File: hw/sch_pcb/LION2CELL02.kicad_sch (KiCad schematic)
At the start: 61 parts, among them J1 JUMP_4X2, J13 JUMP_4X2, J15 CONN_2, J2 JUMP_2x1, J3 JUMP_2x1, J4 JUMP2_2x1, J5 JUMP_2x1, J6 JUMP_2x1, J7 JUMP_4X2, J8 CONN1_1, J9 CONN1_1, P1 _, P2 _, P3 _, P4 _, Q1 IRLML6244, U1 BQ29209, U2 BQ24103, U5 TPS76601, U6 APX810-31SAG-7

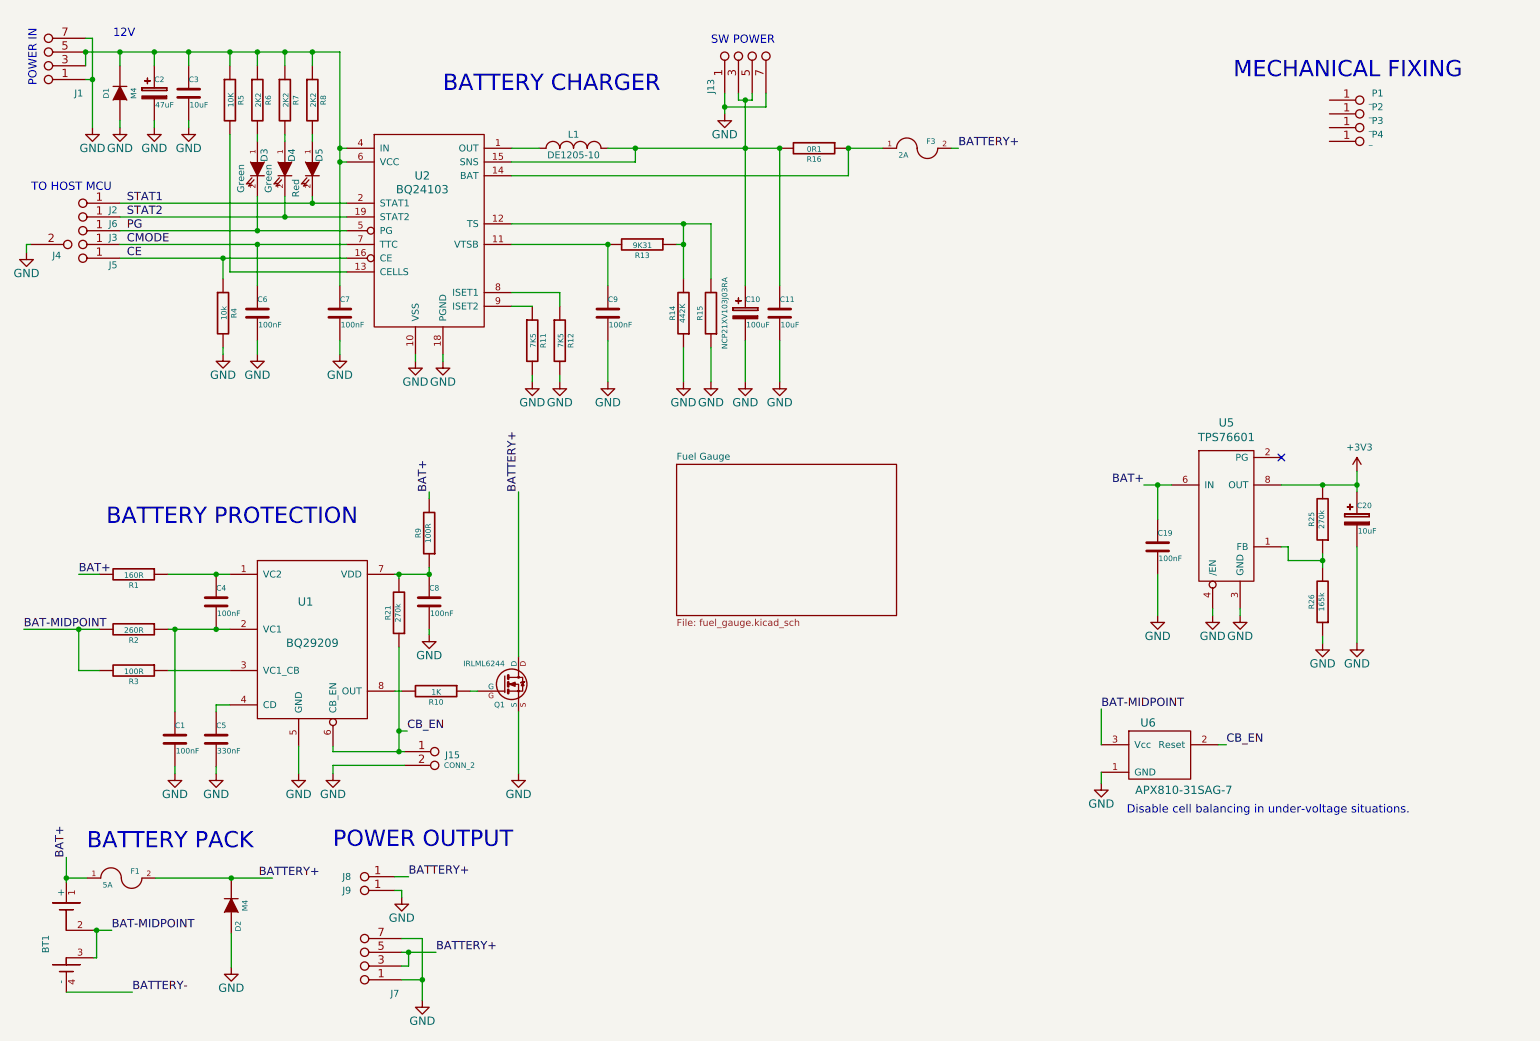
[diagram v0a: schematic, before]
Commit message: Initial work on battery charging.
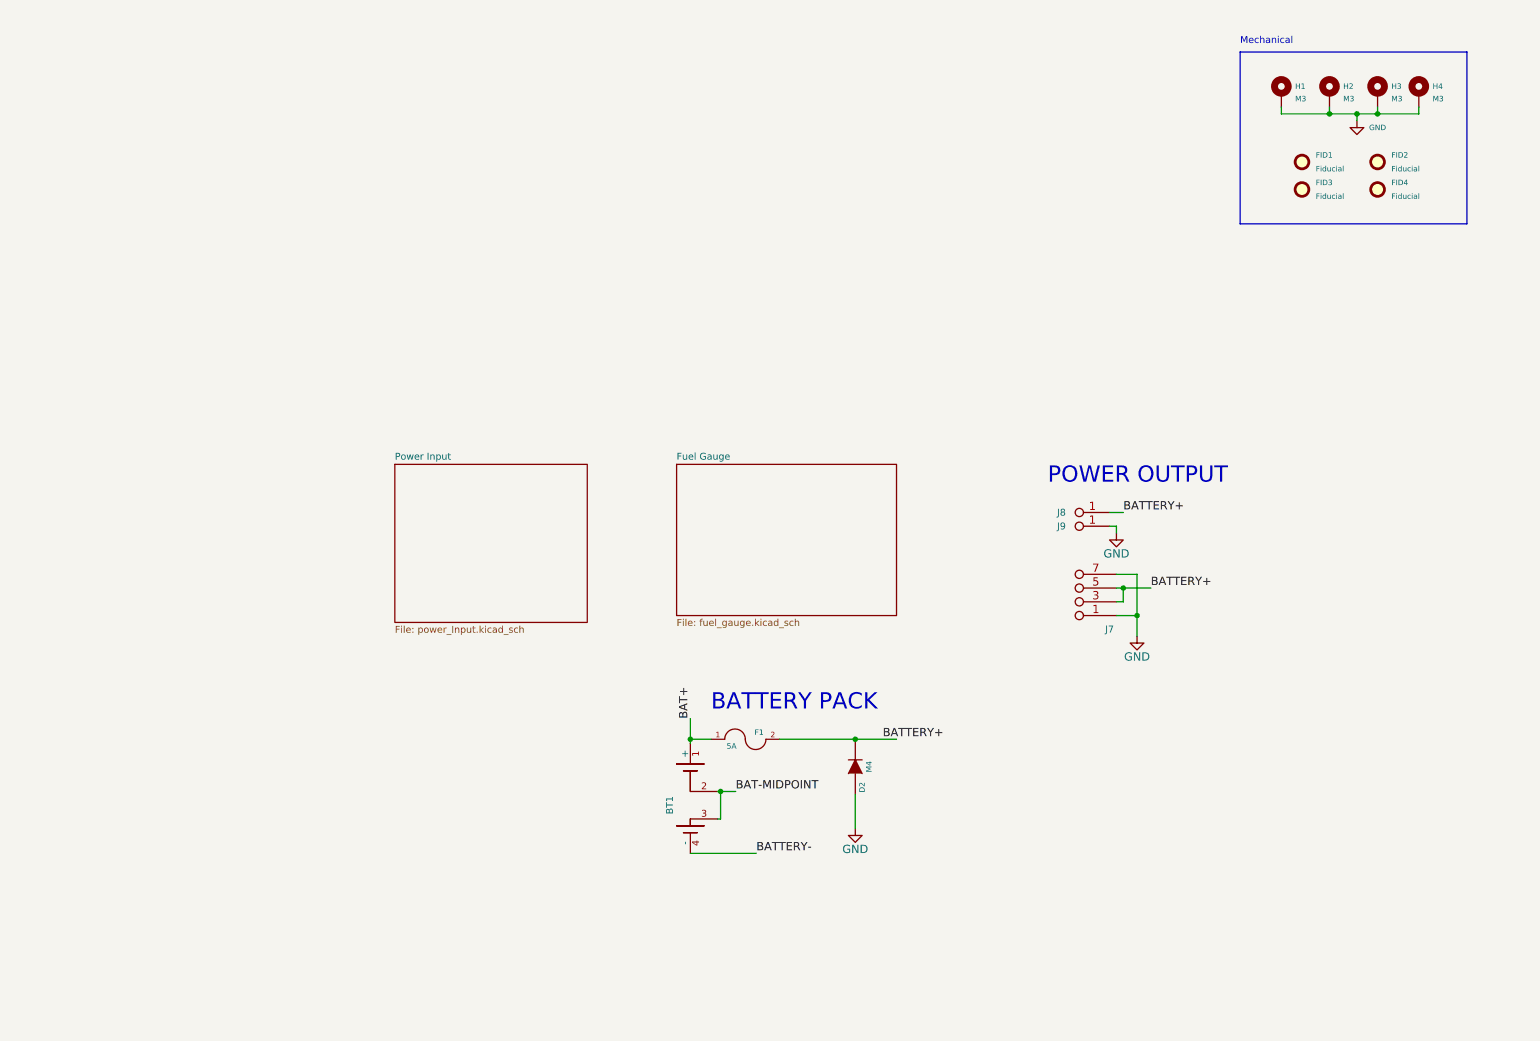
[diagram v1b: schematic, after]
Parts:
- removed C1, C19, C4, C6, C7, C8, C9: 100nF, Mlab_R:SMD-0805, symbol LION2CELL01D-rescue:C-RESCUE-LION2CELL01C
- removed C10: 100uF, Mlab_C:TantalC_SizeD_Reflow, symbol LION2CELL01D-rescue:CP2
- removed C11, C3: 10uF, Mlab_R:SMD-0805, symbol LION2CELL01D-rescue:C-RESCUE-LION2CELL01C
- removed C2: 47uF, Mlab_C:TantalC_SizeC_Reflow, symbol LION2CELL01D-rescue:CP2
- removed C20: 10uF, Mlab_C:TantalC_SizeB_Reflow, symbol LION2CELL01D-rescue:CP2
- removed C5: 330nF, Mlab_R:SMD-0805, symbol LION2CELL01D-rescue:C-RESCUE-LION2CELL01C
- removed D1: M4, Mlab_D:SMA_Standard, symbol LION2CELL01D-rescue:DIODE
- removed D3, D4: Green, Mlab_D:LED_1206, symbol LION2CELL01D-rescue:LED-RESCUE-LION2CELL01C
- removed D5: Red, Mlab_D:LED_1206, symbol LION2CELL01D-rescue:LED-RESCUE-LION2CELL01C
- removed F3: 2A, Mlab_F:Drzak_2410, symbol LION2CELL01D-rescue:FUSE
- removed J1, J13: JUMP_4X2, Mlab_Pin_Headers:Straight_2x04, symbol LION2CELL01D-rescue:JUMP_4X2
- removed J15: CONN_2, Mlab_Pin_Headers:SMD_1_2x2, symbol LION2CELL01D-rescue:CONN_2
- removed J2, J3, J5, J6: JUMP_2x1, Mlab_Pin_Headers:Straight_1x02, symbol LION2CELL01D-rescue:JUMP_2x1
- removed J4: JUMP2_2x1, symbol LION2CELL01D-rescue:JUMP2_2x1
- removed L1: DE1205-10, Mlab_L:DE1205-10, symbol LION2CELL01D-rescue:INDUCTOR_SMALL
- removed P1, P2, P3, P4: _, Mlab_Mechanical:MountingHole_3mm, symbol LION2CELL01D-rescue:_
- removed Q1: IRLML6244, Mlab_T:SOT-23, symbol LION2CELL01D-rescue:MOSFET-N
- removed R1: 160R, Mlab_R:SMD-0805, symbol LION2CELL01D-rescue:R-RESCUE-LION2CELL01C
- removed R10: 1K, Mlab_R:SMD-0805, symbol LION2CELL01D-rescue:R-RESCUE-LION2CELL01C
- removed R11, R12: 7K5, Mlab_R:SMD-0805, symbol LION2CELL01D-rescue:R-RESCUE-LION2CELL01C
- removed R13: 9K31, Mlab_R:SMD-0805, symbol LION2CELL01D-rescue:R-RESCUE-LION2CELL01C
- removed R14: 442K, Mlab_R:SMD-0805, symbol LION2CELL01D-rescue:R-RESCUE-LION2CELL01C
- removed R15: NCP21XV103J03RA, Mlab_R:SMD-0805, symbol LION2CELL01D-rescue:R-RESCUE-LION2CELL01C
- removed R16: 0R1, Resistors_SMD:R_2512, symbol LION2CELL01D-rescue:R-RESCUE-LION2CELL01C
- removed R2: 260R, Mlab_R:SMD-0805, symbol LION2CELL01D-rescue:R-RESCUE-LION2CELL01C
- removed R21, R25: 270k, Mlab_R:SMD-0805, symbol LION2CELL01D-rescue:R-RESCUE-LION2CELL01C
- removed R26: 165k, Mlab_R:SMD-0805, symbol LION2CELL01D-rescue:R-RESCUE-LION2CELL01C
- removed R3, R9: 100R, Mlab_R:SMD-0805, symbol LION2CELL01D-rescue:R-RESCUE-LION2CELL01C
- removed R4: 10k, Mlab_R:SMD-0805, symbol LION2CELL01D-rescue:R-RESCUE-LION2CELL01C
- removed R5: 10K, Mlab_R:SMD-0805, symbol LION2CELL01D-rescue:R-RESCUE-LION2CELL01C
- removed R6, R7, R8: 2K2, Mlab_R:SMD-0805, symbol LION2CELL01D-rescue:R-RESCUE-LION2CELL01C
- removed U1: BQ29209, Mlab_IO:VSON-8, symbol LION2CELL01D-rescue:BQ29209
- removed U2: BQ24103, Mlab_IO:VQFN-20, symbol LION2CELL01D-rescue:BQ24103
- removed U5: TPS76601, Mlab_IO:SO-8, symbol LION2CELL01D-rescue:TPS76601
- removed U6: APX810-31SAG-7, Mlab_IO:SOT-23, symbol LION2CELL01D-rescue:APX810-31SAG-7
- added FID1, FID2, FID3, FID4: Fiducial, Fiducial:Fiducial_1mm_Mask2mm, symbol Mechanical:Fiducial
- added H1, H2, H3, H4: M3, Mlab_Mechanical:MountingHole_3mm, symbol Mechanical:MountingHole_Pad
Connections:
- net GND: now also H1.1, H2.1, H3.1, H4.1
- no-connect marks 1 -> 0
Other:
- added sheet Power Input (power_Input.kicad_sch)
- note added: "Mechanical"
- note removed: "12V"
- note removed: "BATTERY CHARGER"
- note removed: "BATTERY PROTECTION"
- note removed: "Disable cell balancing in under-voltage situations."
- note removed: "MECHANICAL FIXING"
- note removed: "POWER IN"
- note removed: "SW POWER"
- note removed: "TO HOST MCU"
- moved on the sheet: BT1, D2, F1, J7, J8, J9

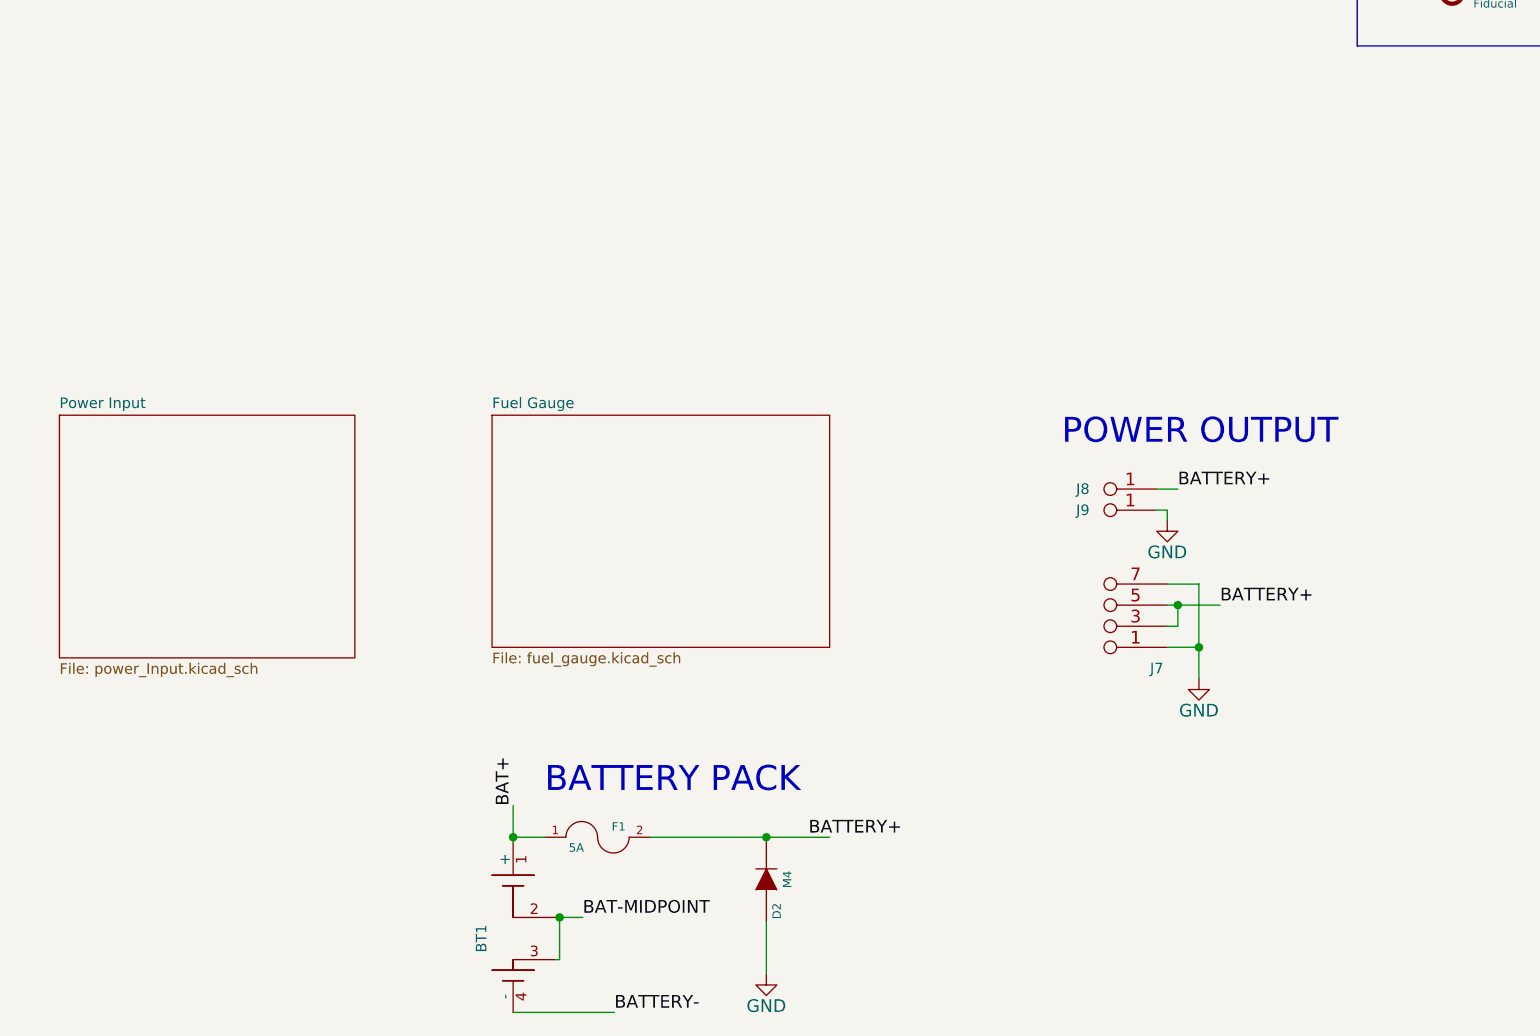
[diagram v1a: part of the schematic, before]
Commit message: work of the schematics of charger completed.
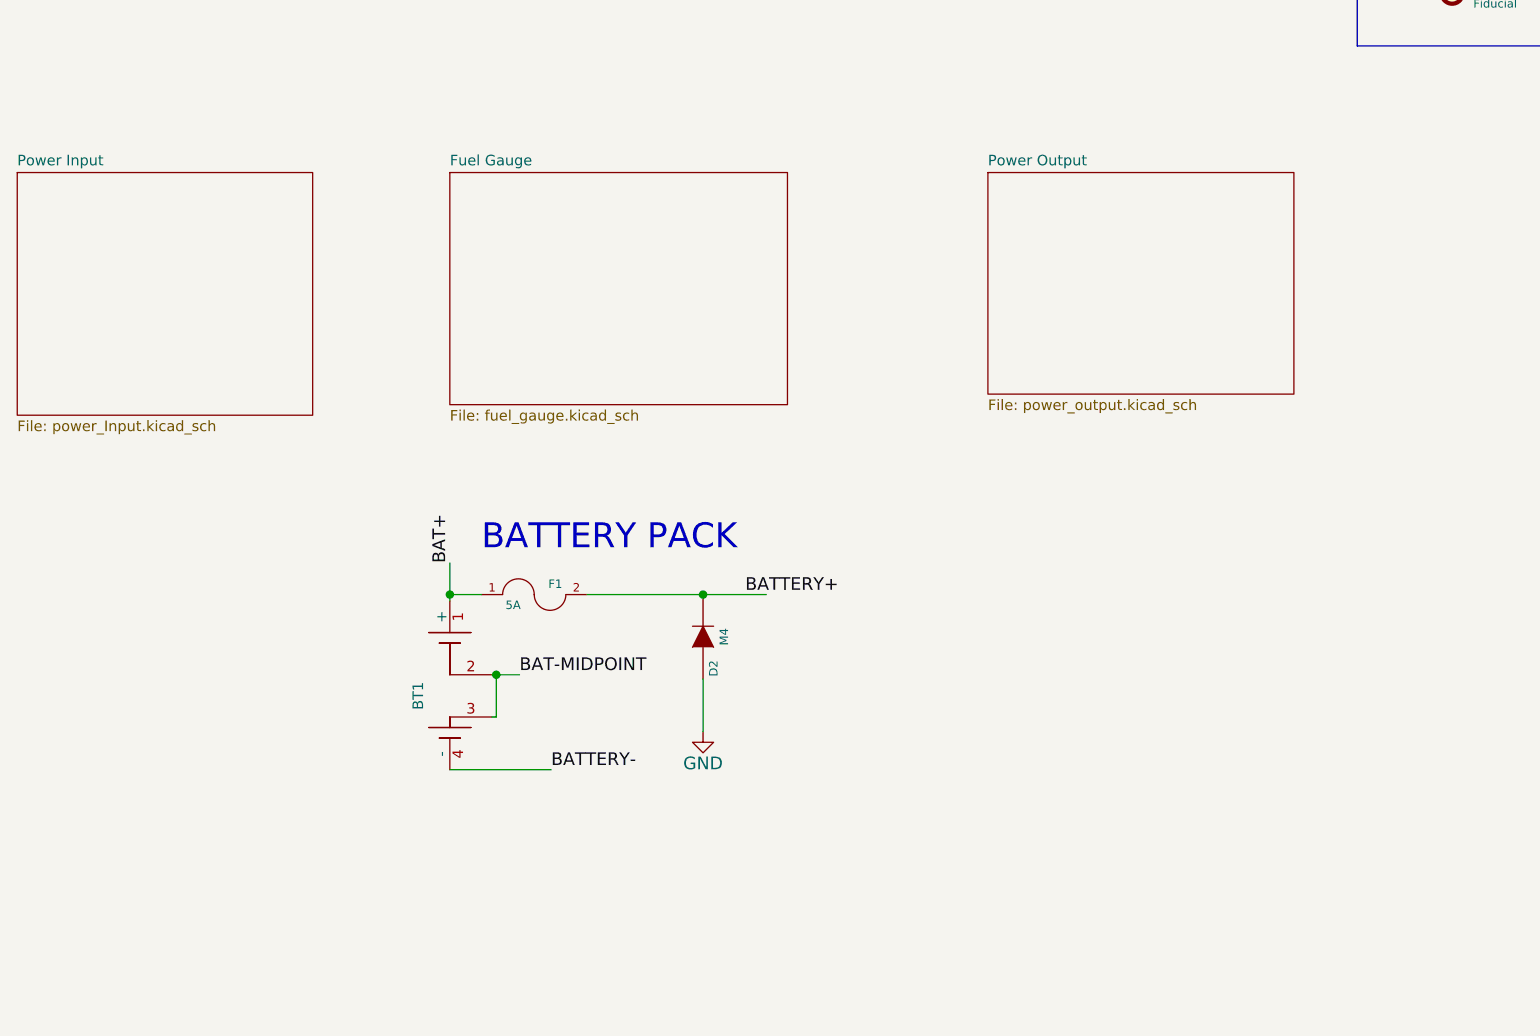
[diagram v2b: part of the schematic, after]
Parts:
- removed J7: JUMP_4X2, Mlab_Pin_Headers:Straight_2x04, symbol LION2CELL01D-rescue:JUMP_4X2
- removed J8, J9: CONN1_1, Mlab_Con:WAGO256, symbol LION2CELL01D-rescue:CONN1_1
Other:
- added sheet Power Output (power_output.kicad_sch)
- note removed: "POWER OUTPUT"
- moved on the sheet: BT1, D2, F1
